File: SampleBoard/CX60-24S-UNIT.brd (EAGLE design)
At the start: 30.5 x 40.6 mm, 5 parts, among them CN1 CX60-24S-UNIT, CN2 87520-0010BLF, CN3 IF_5PIN_H

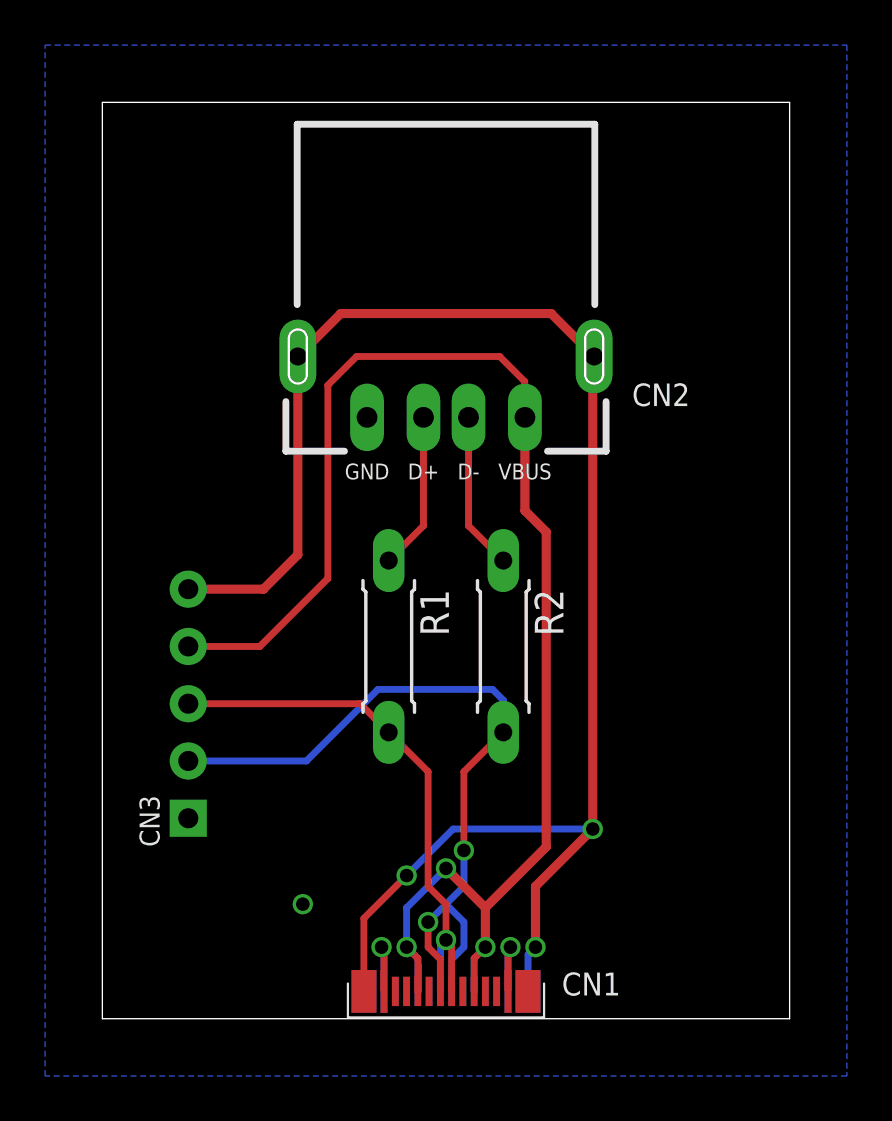
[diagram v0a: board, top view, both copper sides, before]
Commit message: 評価用基板を修正
・CCの配線（プルダウン抵抗）が抜けていたので追加
・テスト用ホールの位置を修正
・プラグB面のD+、D-は不要なので削除
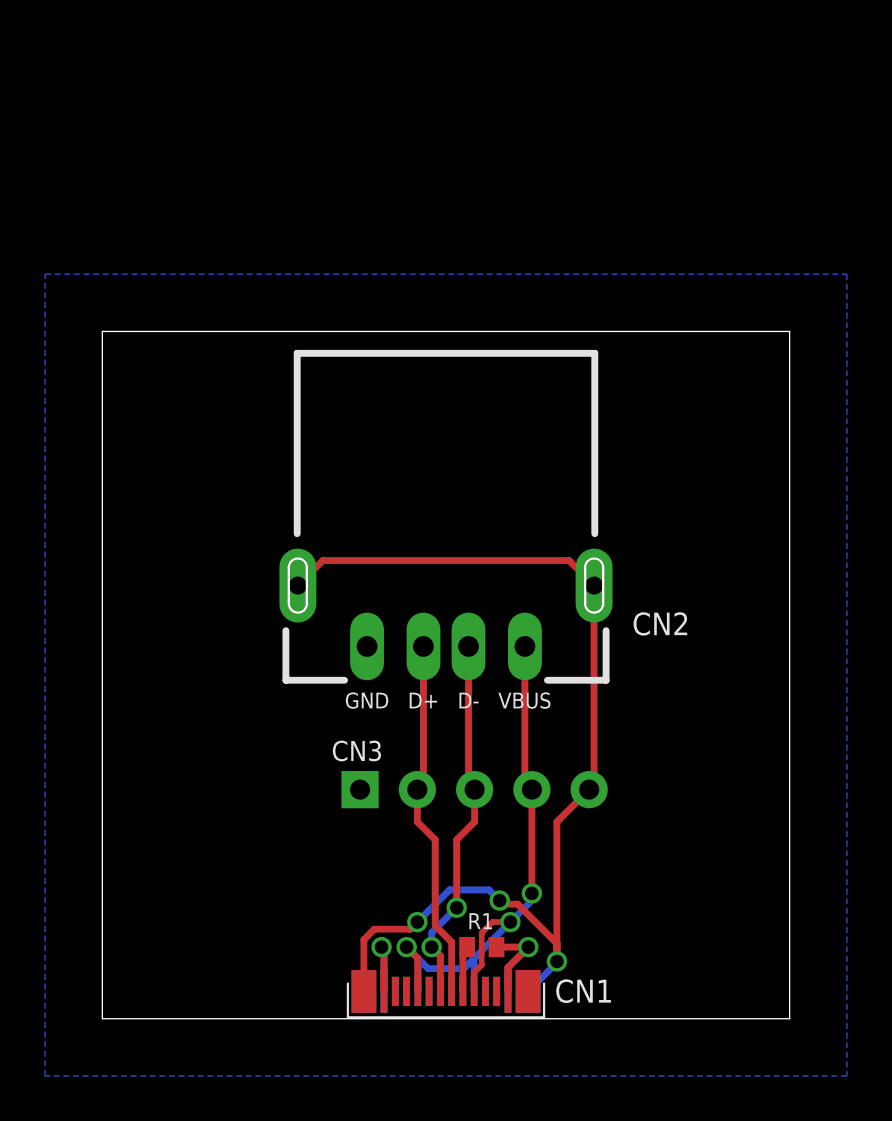
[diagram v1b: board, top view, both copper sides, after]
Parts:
- removed R2: 0R, Parts:RESISTOR_0207_300MIL
- R1: value 0R -> 5.1k; device Parts:RESISTOR_0207_300MIL -> Parts:R0402
- moved R1 17.6 mm to (16.8, 3.17), turned to 180 degrees
- moved CN2 10.2 mm to (15.2, 16.5)
- moved CN3 7.73 mm to (11.4, 10.2), turned to 0 degrees
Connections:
- removed net N$1: CN2.D-, R2.1
- removed net N$2: CN2.D+, R1.1
- new net N$3: CN1.A5, R1.2
- net 0V: now also R1.1
- net DN_C: now also CN2.D-, CN3.3; no longer CN1.B7, CN3.2, R2.2
- net DP_C: now also CN2.D+, CN3.2; no longer CN1.B6, CN3.3, R1.2
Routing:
- net VBUS_C: track 69.5 -> 27.9 mm
- net FG_C: track 73.4 -> 47.0 mm
- net DN_C: track 34.4 -> 16.4 mm
- net DP_C: track 24.5 -> 16.0 mm, vias 1 -> 0
- net N$1: track 6.99 -> 0.00 mm
- net N$2: track 6.99 -> 0.00 mm
- net 0V: track 8.04 -> 10.1 mm, vias 3 -> 2
- net N$3: track 0.00 -> 2.04 mm
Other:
- board size 30.5 x 40.6 mm -> 30.5 x 30.5 mm

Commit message: 評価用基板を修正
・配線パターンを修正
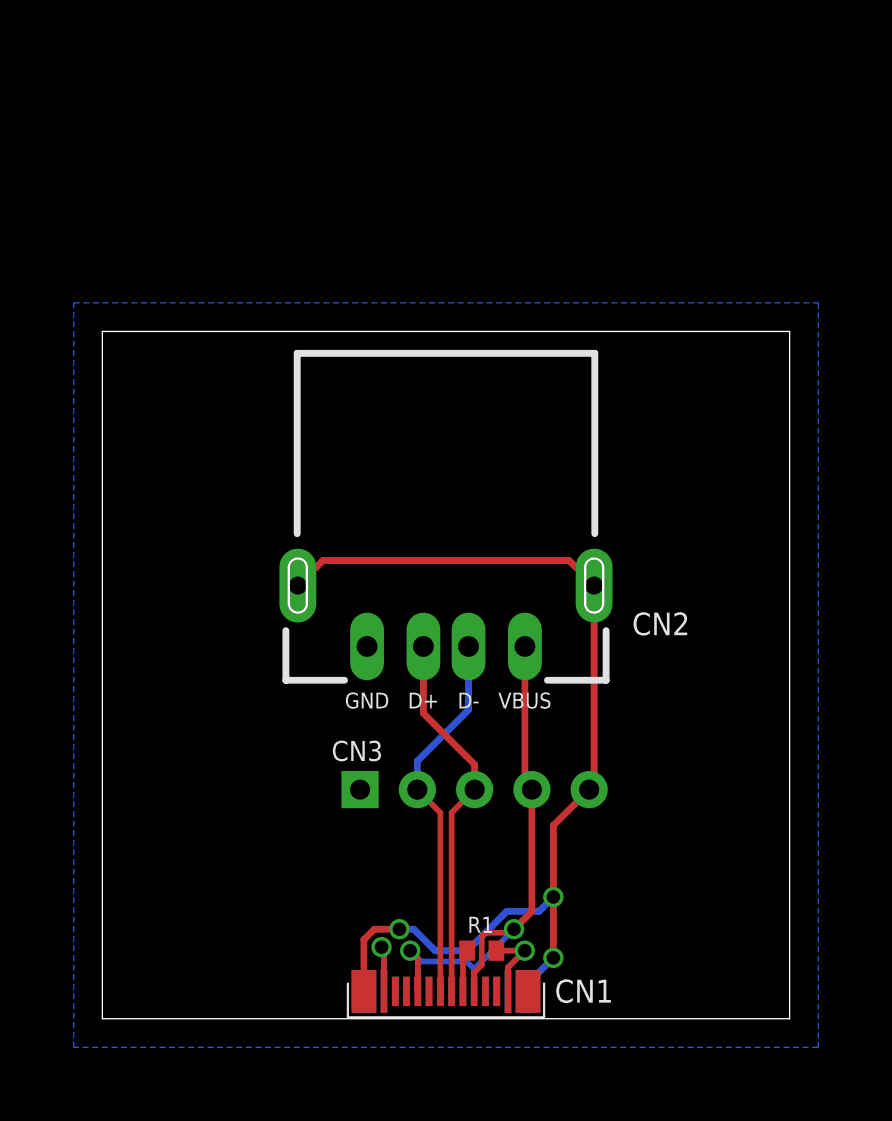
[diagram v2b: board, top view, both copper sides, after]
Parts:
- moved R1 0.16 mm to (16.8, 3.02)
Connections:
- net DN_C: now also CN3.2; no longer CN3.3
- net DP_C: now also CN3.3; no longer CN3.2
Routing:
- net FG_C: track 47.0 -> 45.7 mm
- net DP_C: track 16.0 -> 16.7 mm
- net 0V: track 10.1 -> 9.50 mm
- net DN_C: track 16.4 -> 16.7 mm, vias 2 -> 0
- net VBUS_C: track 27.9 -> 27.7 mm, vias 3 -> 2
